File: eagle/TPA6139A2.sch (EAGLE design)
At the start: 12 parts

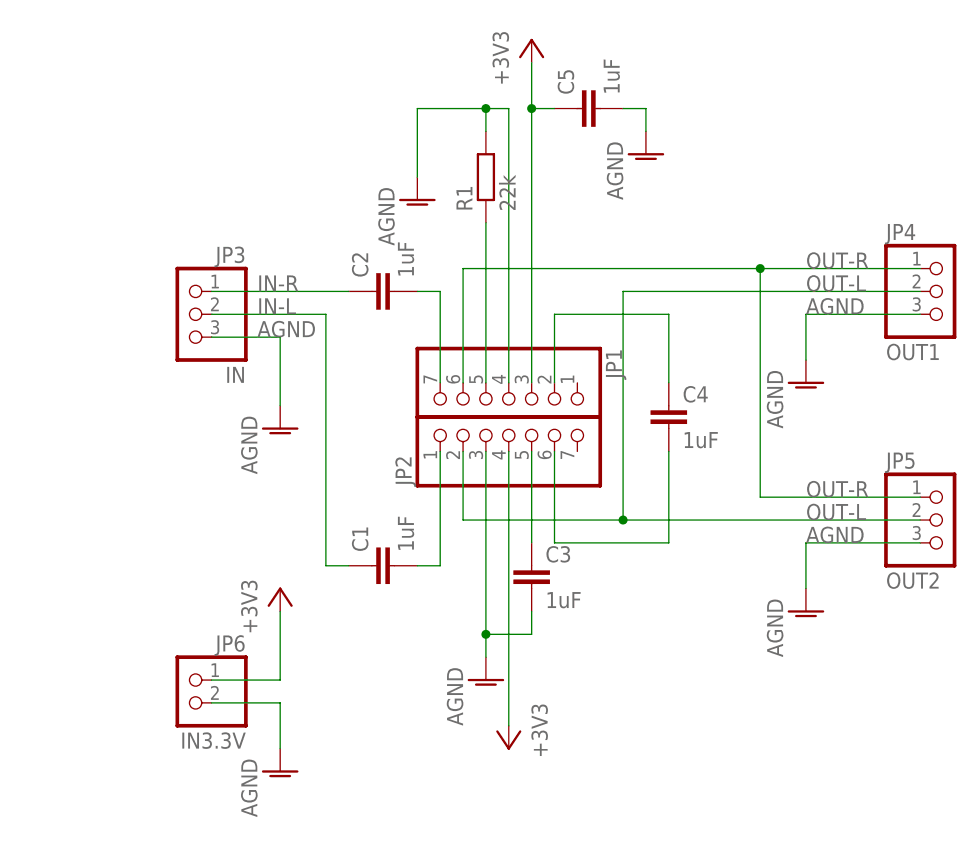
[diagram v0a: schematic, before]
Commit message: 回路図、基板図修正
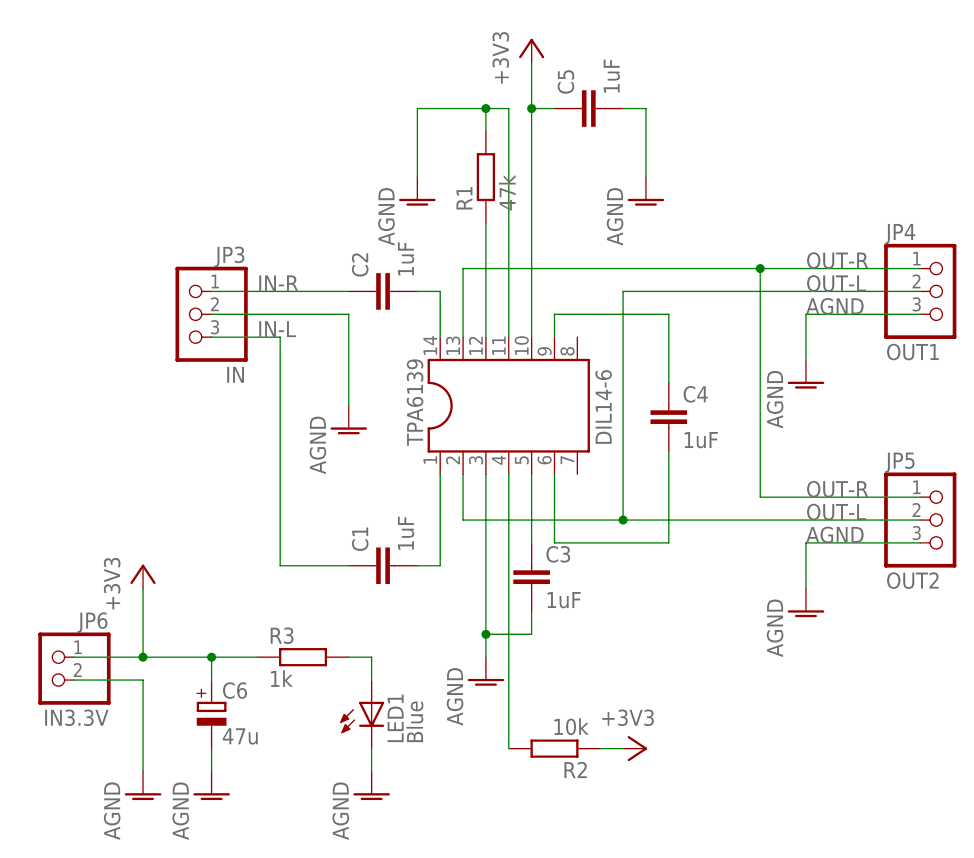
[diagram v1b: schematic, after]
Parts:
- removed JP1, JP2: (no value), pinhead:PINHD-1X7
- added C6: 47u, rcl:CPOL-EUTT2D5L
- added LED1: Blue, led:LED3MM
- added R2: 10k, rcl:R-EU_0207/7
- added R3: 1k, rcl:R-EU_0207/7
- added TPA6139: DIL14-6, mylib:DIL14-6
- R1: value 22k -> 47k
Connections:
- removed net N$11: JP1.5, R1.1
- new net N$3: R2.2, TPA6139.4
- new net N$4: C3.1, TPA6139.5
- new net N$5: R1.1, TPA6139.12
- net +3V3: now also C6.+, R2.1, R3.1, TPA6139.10; no longer JP1.3, JP2.4
- net AGND: now also C6.-, JP3.2, LED1.C, TPA6139.11, TPA6139.3; no longer JP1.4, JP2.3, JP3.3
- net IN-L: now also JP3.3; no longer JP3.2
- net N$1: now also TPA6139.14; no longer JP1.7
- net N$10: now also TPA6139.9; no longer JP1.2
- net N$2: now also TPA6139.1; no longer JP2.1
- net N$6: now also LED1.A, R3.2; no longer C3.1, JP2.5
- net N$9: now also TPA6139.6; no longer JP2.6
- net OUT-L: now also TPA6139.2; no longer JP2.2
- net OUT-R: now also TPA6139.13; no longer JP1.6
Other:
- moved on the sheet: JP6
